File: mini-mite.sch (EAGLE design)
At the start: 27 parts, among them IC2 LM7805, Q1 2N2222, Q2 2N2907, Q3 IRF2804, Q4 IRF2804, U1 ATTiny13

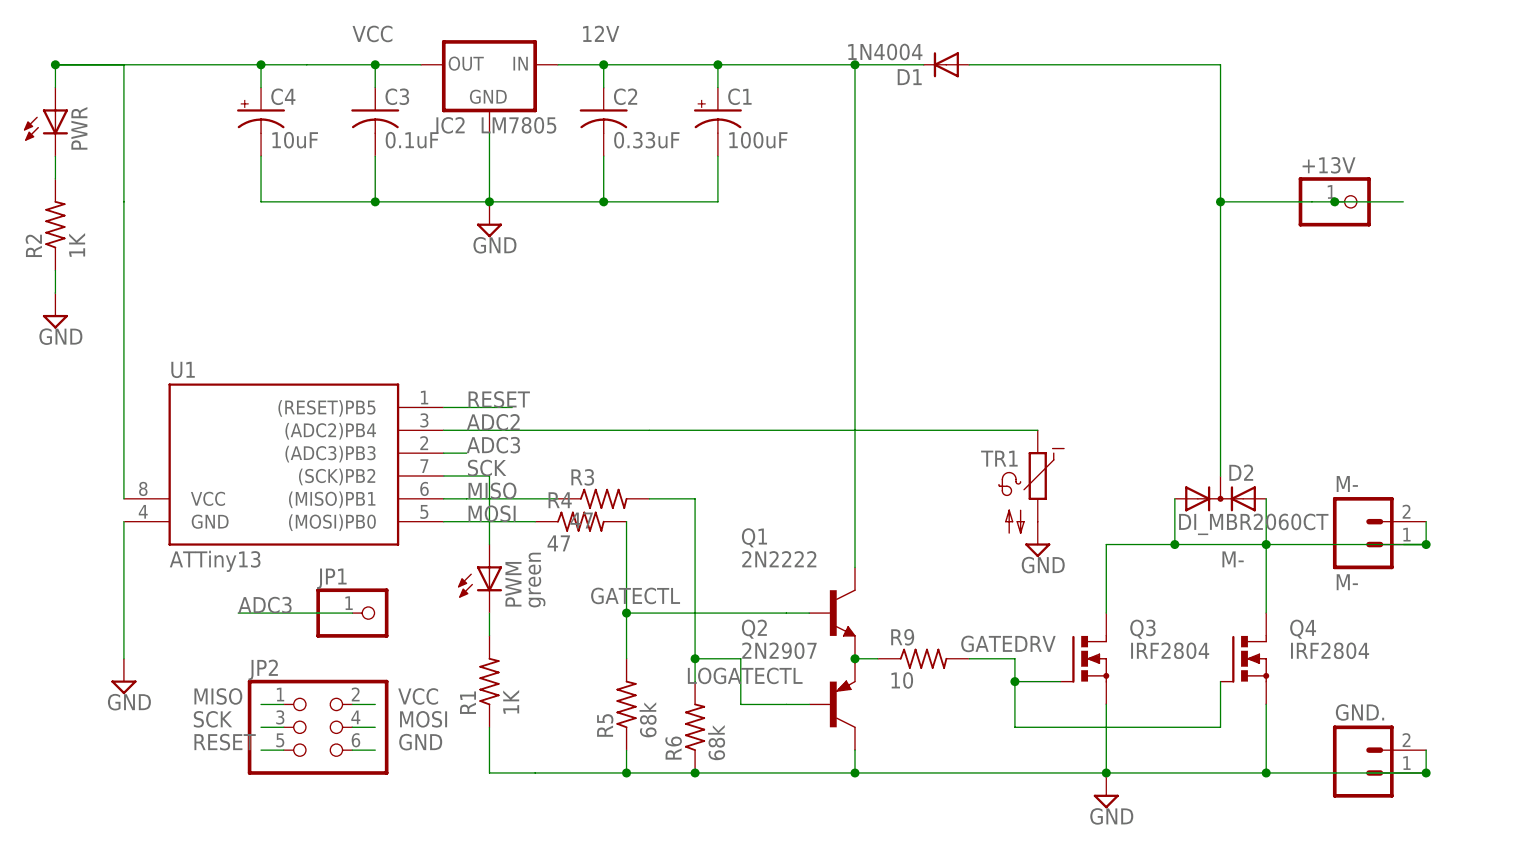
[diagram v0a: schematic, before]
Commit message: Fixed drive voltage range bug.
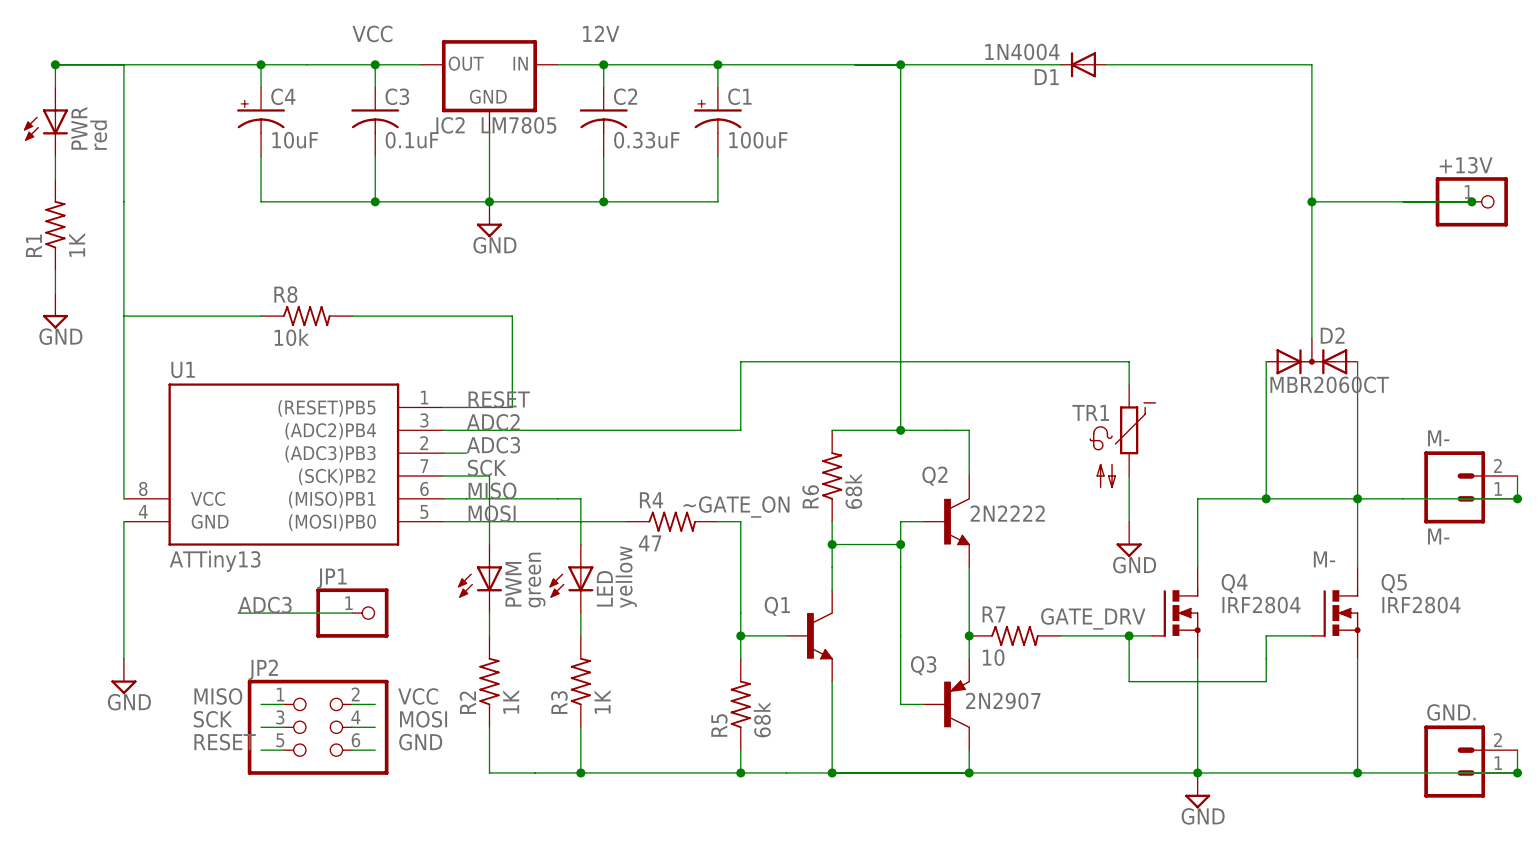
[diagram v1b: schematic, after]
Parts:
- removed R9: 10, resistor:R-US_0207/2V
- added LED: yellow, led:LED5MM
- added Q5: IRF2804, transistor-power:PMOSFET_NTO220BV
- added R7: 10, resistor:R-US_0207/7
- added R8: 10k, resistor:R-US_0207/7
- D2: value DI_MBR2060CT -> MBR2060CT
- PWR: value (none) -> red
- Q1: device transistor:2N2222 -> adafruit:2N2222
- Q2: value 2N2907 -> 2N2222; device transistor-pnp:2N2907 -> adafruit:2N2222
- Q3: value IRF2804 -> 2N2907; device transistor-power:PMOSFET_NTO220BV -> adafruit:2N2907
- R3: value 47 -> 1K
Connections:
- net GATECTL renamed ~GATE_ON
- removed net GATEDRV: Q3.G, Q4.G, R9.2
- removed net LOGATECTL: Q2.B, R3.2, R6.2
- removed net N$3: Q1.E, Q2.E, R9.1
- new net GATEON: Q1.C, Q2.B, Q3.B, R6.1
- new net GATE_DRV: Q4.G, Q5.G, R7.2
- new net N$1: LED.C, R3.2
- new net N$4: Q2.E, Q3.E, R7.1
- net 12V: now also Q2.C, R6.2; no longer Q1.C
- net GND: now also Q1.E, Q3.C, Q5.S, R3.1; no longer Q2.C, Q3.S, R6.1
- net M-: now also Q5.D; no longer Q3.D
- net MISO: now also LED.A; no longer R3.1
- net N$19: now also R2.2; no longer R1.2
- net N$5: now also R1.2; no longer R2.2
- net RESET: now also R8.2
- net VCC: now also R8.1
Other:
- moved on the sheet: +13V, D1, D2, GND., M-, Q1, Q4, R1, R2, R3, R4, R5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
